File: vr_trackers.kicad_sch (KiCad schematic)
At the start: 57 parts, among them SW2 TS-1088-AR02016, U1 nRF52840, U2 TPS63001DRCR, U3 MAX40203AUK+T, U4 MAX40203AUK+T, U5 LSM6DSVQTR, U6 BMM350_C17225907, U7 XL7EL89COI-111YLC-32M, U8 BQ24075RGTR, U9 MAX17048G+T10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

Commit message: add firmware stuff and update the pcb
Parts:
- C1: LCSC Part (none) -> C140782
- C11, C18, C20: LCSC Part (none) -> C60474
- C12: LCSC Part (none) -> C106200
- C13, C17, C22: LCSC Part (none) -> C23733
- C14: LCSC Part (none) -> C368599
- C15: LCSC Part (none) -> C14445
- C16: LCSC Part (none) -> C161159
- C19: LCSC Part (none) -> C170151
- C2, C23: LCSC Part (none) -> C315248
- C3, C4, C5, C6: LCSC Part (none) -> C76948
- C7: LCSC Part (none) -> C327032
- C8: LCSC Part (none) -> C76912
- L2: LCSC Part (none) -> C395070
- L3: LCSC Part (none) -> C76798
- L4: LCSC Part (none) -> C86059
- R10, R11: LCSC Part (none) -> C105872
- R12, R13: LCSC Part (none) -> C114765
- R2: LCSC Part (none) -> C106231
- R6, R7: LCSC Part (none) -> C105871
- R8: LCSC Part (none) -> C5126026
- R9: LCSC Part (none) -> C2480411
- TH1: LCSC Part (none) -> C77131
- U1: LCSC Part (none) -> C190794

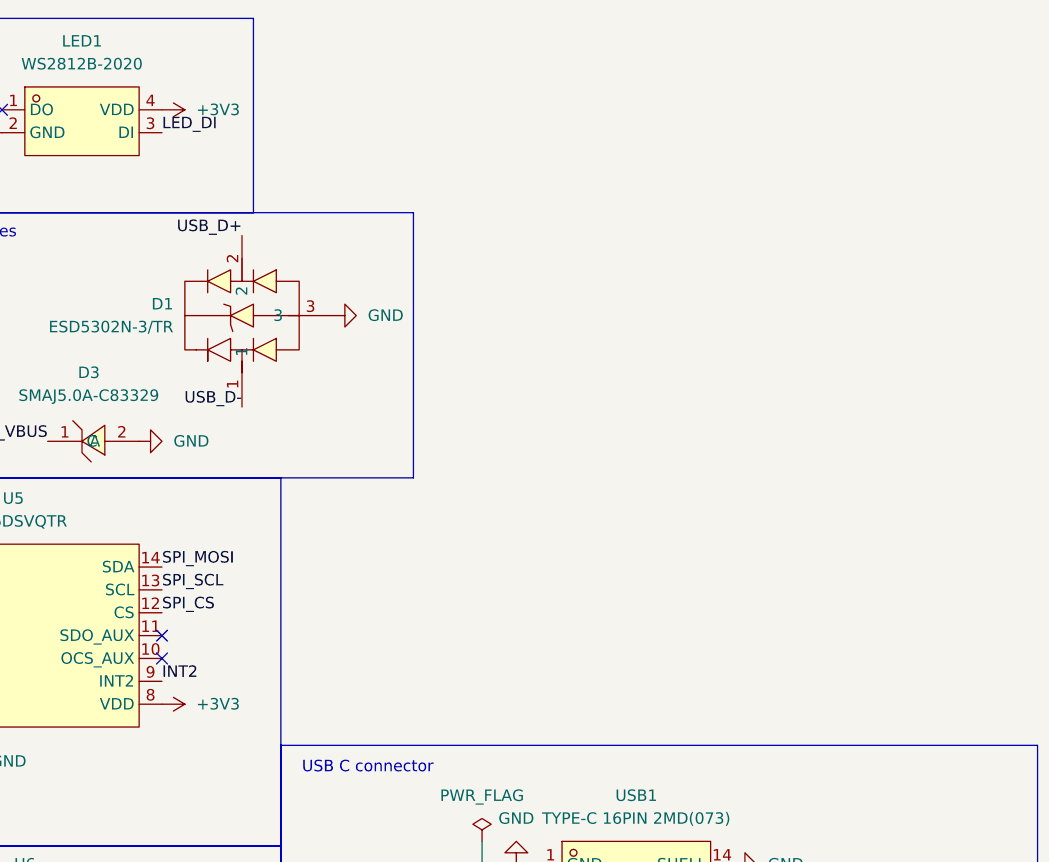
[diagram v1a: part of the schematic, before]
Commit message: Update the pcb to add a 4.5v lane, add a lot to the code, and make a second pcb to help programming
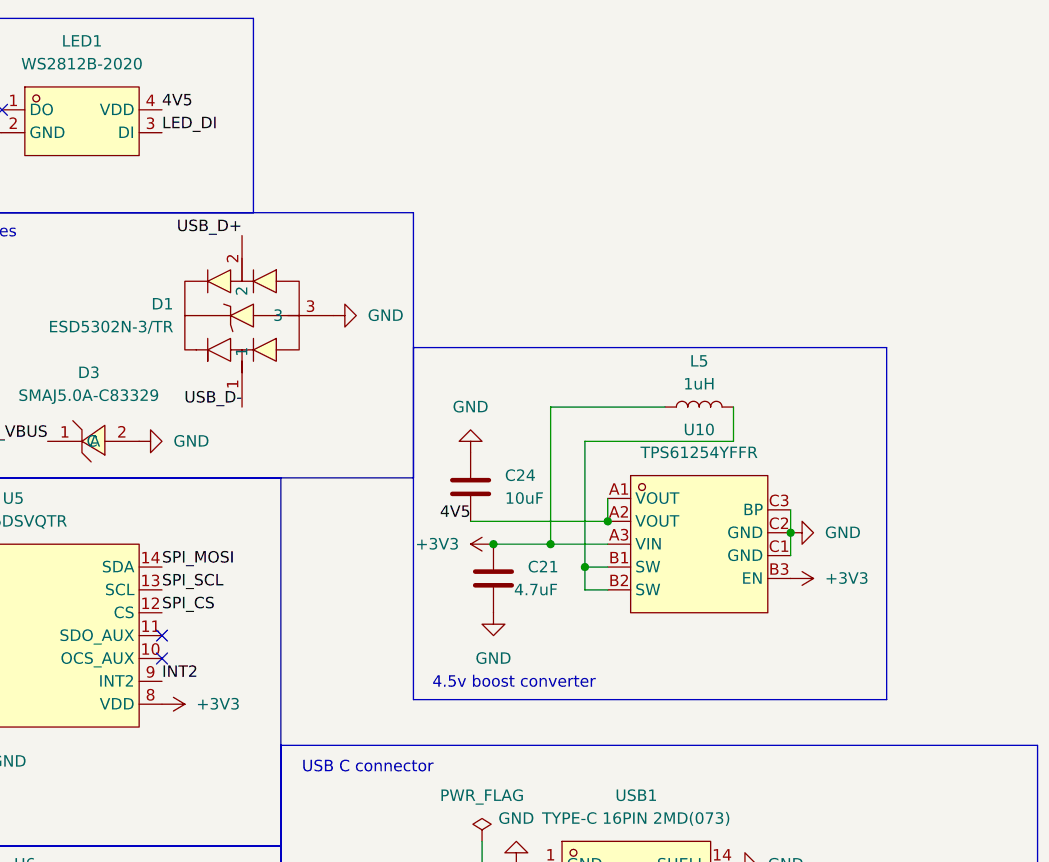
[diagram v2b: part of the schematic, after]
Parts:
- added C21: 4.7uF, Capacitor_SMD:C_0402_1005Metric, symbol Device:C
- added C24: 10uF, Capacitor_SMD:C_0402_1005Metric, symbol Device:C
- added L5: 1uH, Inductor_SMD:L_0402_1005Metric, symbol Device:L
- added U10: TPS61254YFFR, easyeda2kicad:DSBGA-9_L1.3-W1.3-R3-C3-P0.40-BL, symbol easyeda2kicad:TPS61254YFFR
- C1: digikey (none) -> 490-13247-1-ND
- C2, C23: digikey (none) -> 490-GRM155R61A106ME11DCT-ND
- C3, C4, C5, C6: digikey (none) -> 399-C0402C120J5GACTUCT-ND
- C7: digikey (none) -> 490-11253-1-ND
- C8: digikey (none) -> 490-11250-1-ND
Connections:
- net +3V3: now also C21.2, L5.1, U10.A3 (VIN), U10.B3 (EN); no longer LED1.4 (VDD)
- net GND: now also C21.1, C24.1, U10.C1 (GND), U10.C2 (GND), U10.C3 (BP)
- new net: L5.2, U10.B1 (SW), U10.B2 (SW)
- new net 4V5: C24.2, LED1.4 (VDD), U10.A1 (VOUT), U10.A2 (VOUT)
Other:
- note added: "4.5v boost converter"
